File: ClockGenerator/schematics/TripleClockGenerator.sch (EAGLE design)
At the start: 39 parts, among them IC1 MEGA168, Q1 2N3904, Q2 2N3904, Q3 2N3904, Y1 16Mhz

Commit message: Rev04
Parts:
- added JP2: (no value), pinhead:PINHD-1X3
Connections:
- net GND: now also JP2.2
- net N$11: now also JP2.3
- net N$15: now also JP2.1
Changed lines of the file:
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@@
 <part name="P2" library="Rebel" deviceset="POT-BOURNS-PTD901" device=""/>
 <part name="P3" library="Rebel" deviceset="POT-BOURNS-PTD901" device=""/>
+<part name="JP2" library="pinhead" deviceset="PINHD-1X3" device=""/>
+<part name="GND3" library="supply1" deviceset="GND" device=""/>
 </parts>
 <sheets>
@@
 <instance part="P2" gate="G$1" x="147.32" y="91.44"/>
 <instance part="P3" gate="G$1" x="167.64" y="91.44"/>
+<instance part="JP2" gate="A" x="106.68" y="63.5"/>
+<instance part="GND3" gate="1" x="99.06" y="55.88"/>
 </instances>
 <busses>
@@
 <wire x1="226.06" y1="27.94" x2="226.06" y2="35.56" width="0.1524" layer="91"/>
 </segment>
+<segment>
+<pinref part="JP2" gate="A" pin="2"/>
+<pinref part="GND3" gate="1" pin="GND"/>
+<wire x1="104.14" y1="63.5" x2="99.06" y2="63.5" width="0.1524" layer="91"/>
+<wire x1="99.06" y1="63.5" x2="99.06" y2="58.42" width="0.1524" layer="91"/>
+</segment>
 </net>
 <net name="+12V" class="0">
@@
 <pinref part="IC1" gate="G$1" pin="PC5(ADC5/SCL)"/>
 <wire x1="81.28" y1="60.96" x2="104.14" y2="60.96" width="0.1524" layer="91"/>
+<pinref part="JP2" gate="A" pin="3"/>
 </segment>
 </net>
@@
 <segment>
 <pinref part="IC1" gate="G$1" pin="PC4(ADC4/SDA)"/>
-<wire x1="81.28" y1="63.5" x2="104.14" y2="63.5" width="0.1524" layer="91"/>
+<wire x1="81.28" y1="63.5" x2="93.98" y2="63.5" width="0.1524" layer="91"/>
 </segment>
 </net>
@@
 <pinref part="IC1" gate="G$1" pin="PC3(ADC3)"/>
 <wire x1="81.28" y1="66.04" x2="104.14" y2="66.04" width="0.1524" layer="91"/>
-</segment>
-</net>
+<pinref part="JP2" gate="A" pin="1"/>
+</segment>
+</net>

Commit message: updated schematic for publishing
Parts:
- R15, R3, R7: value 100 -> 100R
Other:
- note added: "CLK TripleClockGenerator Rev04"
- note added: "Open Source Hardware Published under the GNU GPL Copyright 2018 Rebel Technology"
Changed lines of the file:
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@@
 <?xml version="1.0" encoding="utf-8"?>
 <!DOCTYPE eagle SYSTEM "eagle.dtd">
-<eagle version="7.5.0">
+<eagle version="9.0.0">
 <drawing>
 <settings>
 <setting alwaysvectorfont="no"/>
+<setting keepoldvectorfont="yes"/>
 <setting verticaltext="up"/>
 </settings>
@@
 <part name="Q1" library="transistor-npn" deviceset="2N3904" device=""/>
 <part name="R1" library="rcl" deviceset="R-EU_" device="0204/7" value="1K"/>
-<part name="R3" library="rcl" deviceset="R-EU_" device="0204/7" value="100"/>
+<part name="R3" library="rcl" deviceset="R-EU_" device="0204/7" value="100R"/>
 <part name="R2" library="rcl" deviceset="R-EU_" device="0204/7" value="1K"/>
 <part name="GND16" library="supply1" deviceset="GND" device=""/>
@@
 <part name="Q2" library="transistor-npn" deviceset="2N3904" device=""/>
 <part name="R5" library="rcl" deviceset="R-EU_" device="0204/7" value="1K"/>
-<part name="R7" library="rcl" deviceset="R-EU_" device="0204/7" value="100"/>
+<part name="R7" library="rcl" deviceset="R-EU_" device="0204/7" value="100R"/>
 <part name="R6" library="rcl" deviceset="R-EU_" device="0204/7" value="1K"/>
 <part name="GND17" library="supply1" deviceset="GND" device=""/>
@@
 <part name="Q3" library="transistor-npn" deviceset="2N3904" device=""/>
 <part name="R13" library="rcl" deviceset="R-EU_" device="0204/7" value="1K"/>
-<part name="R15" library="rcl" deviceset="R-EU_" device="0204/7" value="100"/>
+<part name="R15" library="rcl" deviceset="R-EU_" device="0204/7" value="100R"/>
 <part name="R14" library="rcl" deviceset="R-EU_" device="0204/7" value="1K"/>
 <part name="GND8" library="supply1" deviceset="GND" device=""/>
@@
 <sheet>
 <plain>
+<text x="-43.18" y="-22.86" size="3.048" layer="97">Open Source Hardware
+Published under the GNU GPL
+Copyright 2018 Rebel Technology</text>
+<text x="-43.18" y="-5.08" size="3.556" layer="97">CLK TripleClockGenerator Rev04</text>
 </plain>
 <instances>
@@
 <pinref part="LED1" gate="G$1" pin="C"/>
 <junction x="63.5" y="-38.1"/>
-<pinref part="LED1" gate="G$1" pin="C"/>
 </segment>
 </net>
@@
 <pinref part="LED2" gate="G$1" pin="C"/>
 <junction x="137.16" y="-38.1"/>
-<pinref part="LED2" gate="G$1" pin="C"/>
 </segment>
 </net>
@@
 <pinref part="LED3" gate="G$1" pin="C"/>
 <junction x="210.82" y="-38.1"/>
-<pinref part="LED3" gate="G$1" pin="C"/>
 </segment>
 </net>
@@
 </schematic>
 </drawing>
+<compatibility>
+<note version="6.3" minversion="6.2.2" severity="warning">
+Since Version 6.2.2 text objects can contain more than one line,
+which will not be processed correctly with this version.
+</note>
+</compatibility>
 </eagle>

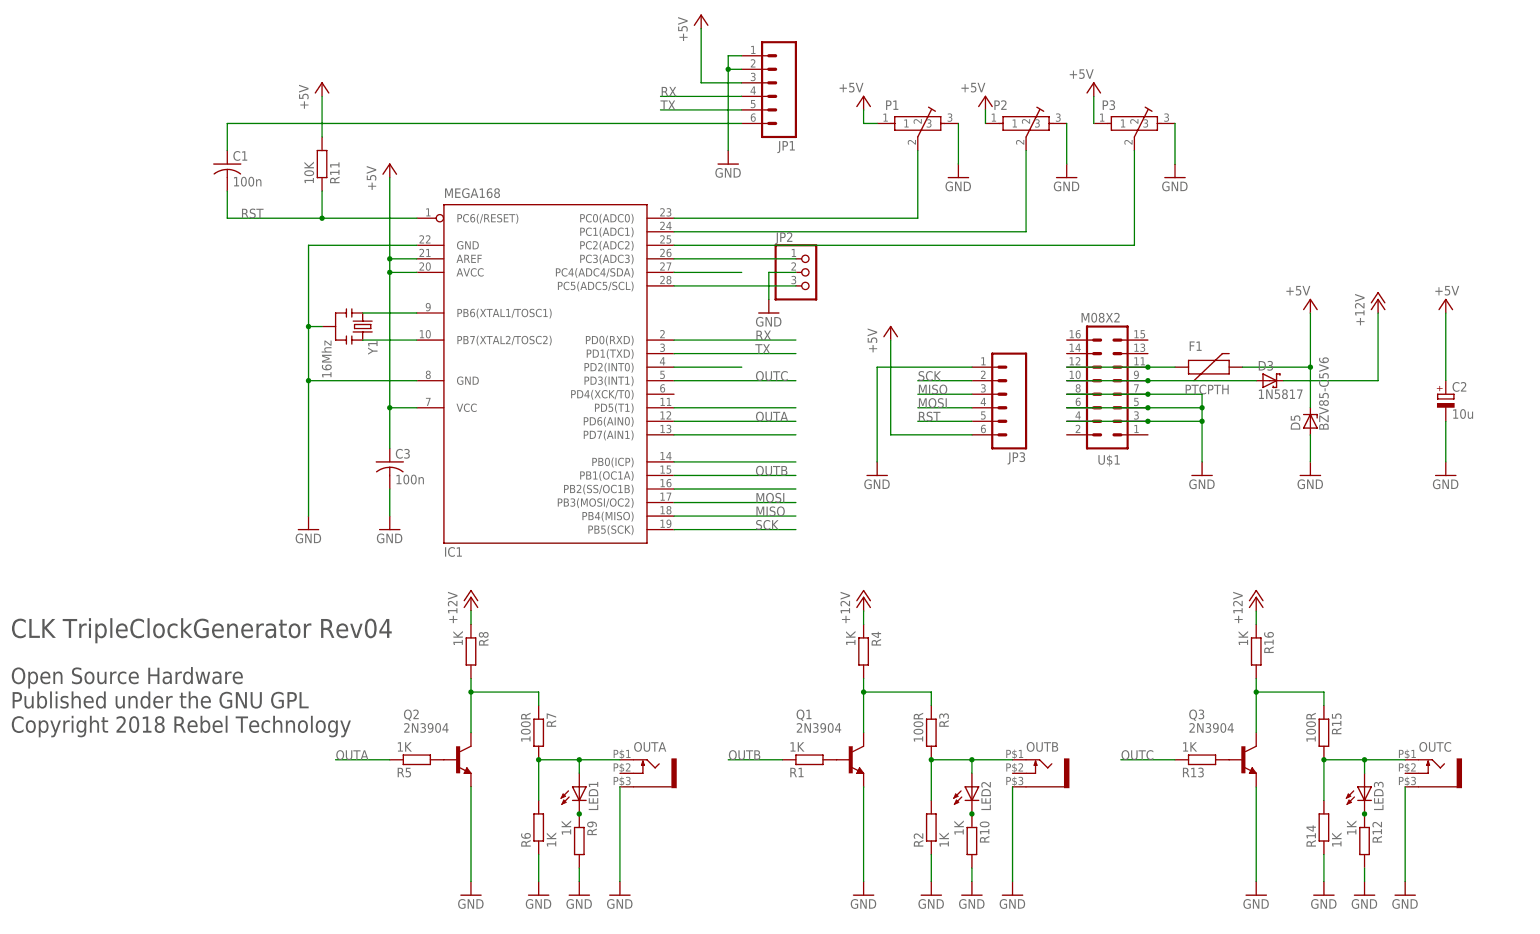
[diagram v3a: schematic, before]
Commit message: Added 5v regulator. Moved pots 0.0125in to edge. Reduced depth. Rev05.
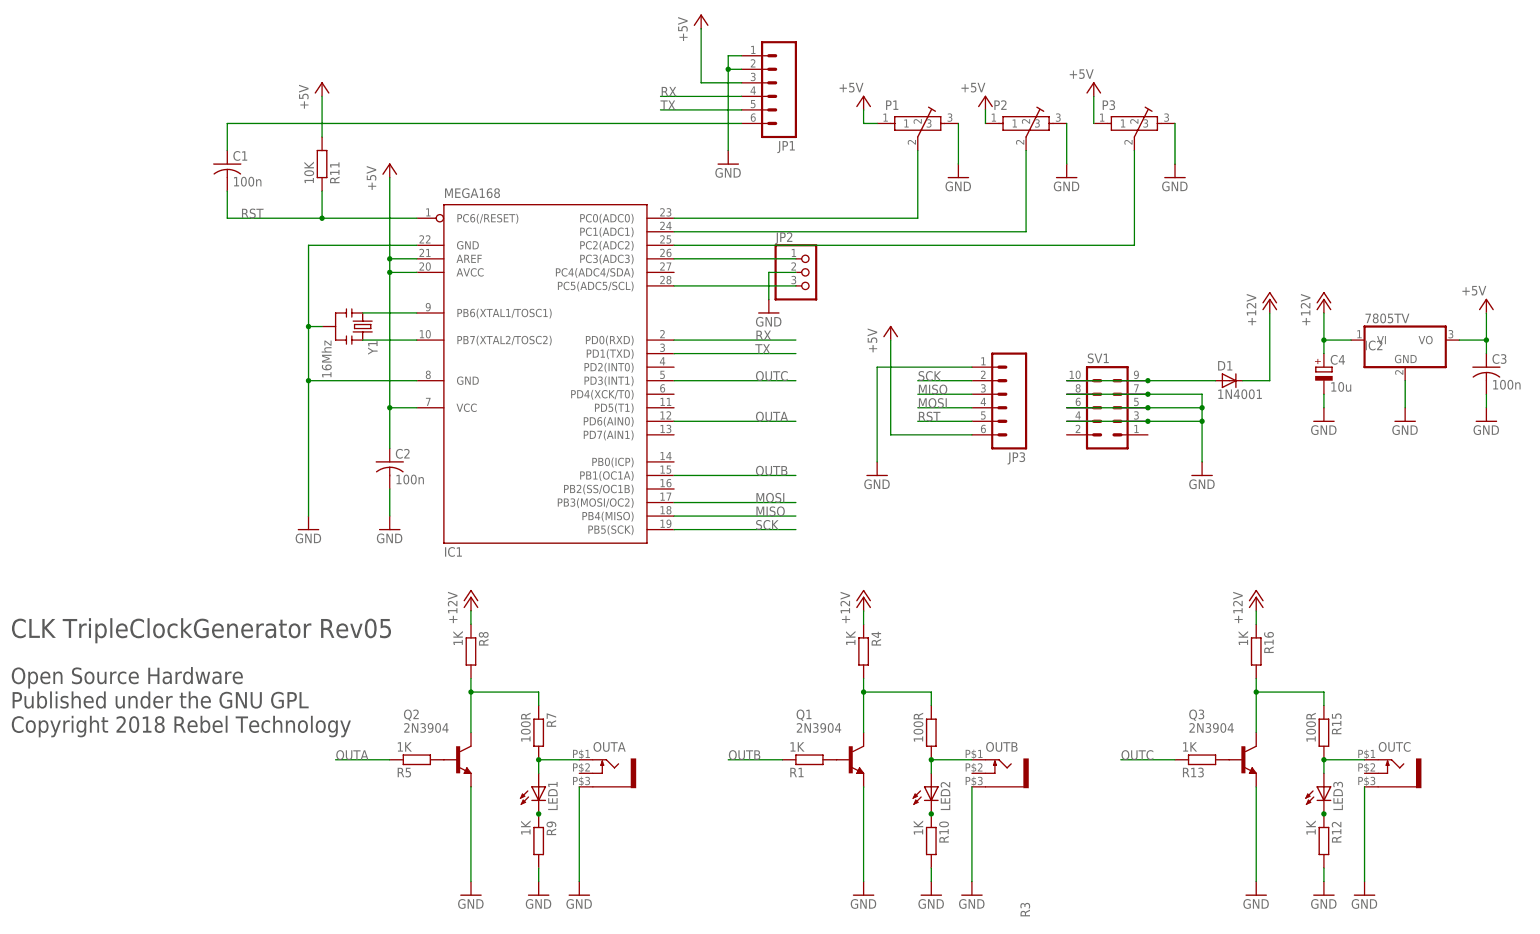
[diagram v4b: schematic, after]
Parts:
- removed D3: 1N5817, diode:1N5819-B
- removed D5: BZV85-C5V6, diode:ZENER-DIODEDO34-7
- removed F1: PTCPTH, Rebel:PTCPTH
- removed R14, R2, R6: 1K, rcl:R-EU_0204/7
- removed U$1: M08X2, SparkFun:M08X2
- added C4: 10u, rcl:CPOL-EUE5-6
- added D1: 1N4001, Rebel:DIODE1N4001
- added IC2: 7805TV, linear:7805TV
- added SV1: (no value), Rebel:MA05-2
- C2: value 10u -> 100n; device rcl:CPOL-EUE5-6 -> rcl:C-US050-024X044
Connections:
- removed net N$10: IC1.PD2(INT0)
- removed net N$12: IC1.PC4(ADC4/SDA)
- removed net N$17: IC1.PD7(AIN1)
- removed net N$19: IC1.PB0(ICP)
- removed net N$44: F1.1, U$1.11, U$1.12
- removed net N$5: IC1.PD5(T1)
- removed net N$6: IC1.PB2(SS/OC1B)
- net +12V: now also C4.+, D1.C, IC2.VI; no longer D3.C
- net +5V: now also C2.1, IC2.VO; no longer C2.+, D5.C, F1.2
- net GND: now also C2.2, C4.-, IC2.GND, SV1.3, SV1.4, SV1.5, SV1.6, SV1.7, SV1.8; no longer C2.-, D5.A, R14.1, R2.1, R6.1, U$1.3, U$1.4, U$1.5, U$1.6, U$1.7, U$1.8
- net N$13: no longer R2.2
- net N$23: no longer R14.2
- net N$26: no longer R6.2
- net N$45: now also D1.A, SV1.10, SV1.9; no longer D3.A, U$1.10, U$1.9
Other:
- note added: "CLK TripleClockGenerator Rev05"
- note removed: "CLK TripleClockGenerator Rev04"
- moved on the sheet: C3, LED1, LED2, LED3, OUTA, OUTB, OUTC, R10, R12, R9
